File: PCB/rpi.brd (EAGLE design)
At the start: 75 x 70 mm, 63 parts, among them IC2 MC1541TO, IC4 MEGA16-A, X1 2526-

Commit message: On branch master 	modified:   PCB/eagle.epf 	modified:   PCB/rpi.brd 	modified:   RaspberryPI/RaspberryPI.pro.user
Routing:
- net GND: track 351.4 -> 365.5 mm
- removed copper zone on layer 1, net N$21
- removed copper zone on layer 16, net N$22
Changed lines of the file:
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@@
 <wire x1="30.45594375" y1="27.49915" x2="30.45594375" y2="24.921153125" width="1.016" layer="1"/>
 <wire x1="30.45594375" y1="24.921153125" x2="32.89613125" y2="22.480965625" width="1.016" layer="1"/>
-<wire x1="57.63515625" y1="25.98173125" x2="57.63515625" y2="21.321634375" width="2.1844" layer="1"/>
 <wire x1="30.45594375" y1="27.49915" x2="32.8984125" y2="29.94161875" width="1.016" layer="1"/>
 <wire x1="32.8984125" y1="29.94161875" x2="32.8984125" y2="33.282871875" width="1.016" layer="1"/>
@@
 <contactref element="C14" pad="-"/>
 <contactref element="C7" pad="-"/>
-<wire x1="57.55154375" y1="14.274546875" x2="57.571628125" y2="14.274546875" width="2.1844" layer="1"/>
-<wire x1="57.571628125" y1="14.274546875" x2="57.571628125" y2="21.25810625" width="2.1844" layer="1"/>
 <wire x1="57.523428125" y1="7.3449" x2="57.523428125" y2="14.24643125" width="2.1844" layer="1"/>
 <wire x1="57.523428125" y1="14.24643125" x2="57.55154375" y2="14.274546875" width="2.1844" layer="1"/>
-<wire x1="57.571628125" y1="21.25810625" x2="57.63515625" y2="21.321634375" width="0" layer="19" extent="1-1"/>
-<wire x1="42.1227" y1="18.626359375" x2="42.12465" y2="10.647703125" width="0" layer="19" extent="1-1"/>
+<wire x1="56.680578125" y1="20.36705625" x2="45.191290625" y2="20.36705625" width="2.1844" layer="1"/>
+<wire x1="45.191290625" y1="20.36705625" x2="44.300240625" y2="21.25810625" width="2.1844" layer="1"/>
+<wire x1="57.571628125" y1="14.29463125" x2="57.571628125" y2="21.25810625" width="2.1844" layer="1"/>
+<wire x1="57.63515625" y1="25.98173125" x2="57.63515625" y2="21.321634375" width="2.1844" layer="1"/>
+<wire x1="57.63515625" y1="21.321634375" x2="57.571628125" y2="21.25810625" width="2.1844" layer="1"/>
+<wire x1="57.571628125" y1="21.25810625" x2="56.680578125" y2="20.36705625" width="2.1844" layer="1"/>
 </signal>
 <signal name="+5V">
@@
 <wire x1="46.23093125" y1="44.331134375" x2="46.443821875" y2="44.544025" width="0.6096" layer="1"/>
 </signal>
-<signal name="N$21">
-<polygon width="0" layer="1" isolate="1.016" thermals="no" rank="6">
-<vertex x="0" y="70"/>
-<vertex x="75" y="70"/>
-<vertex x="75" y="0"/>
-<vertex x="0" y="0"/>
-</polygon>
-</signal>
-<signal name="N$22">
-<polygon width="0" layer="16" isolate="1.016" thermals="no" rank="6">
-<vertex x="0" y="70"/>
-<vertex x="75" y="70"/>
-<vertex x="75" y="0"/>
-<vertex x="0" y="0"/>
-</polygon>
-</signal>
 </signals>

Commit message: On branch master 	modified:   PCB/eagle.epf 	modified:   PCB/rpi.brd 	modified:   PCB/rpi.sch 	modified:   RaspberryPI/mainwindow.cpp 	modified:   RaspberryPI/mainwindow.h 	modified:   RaspberryPI/mainwindow.ui
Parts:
- U$14, U$2: device NX7002AK:SOT23 -> tablet:SOT23
- U$8: device max1811:SO8 -> tablet:SO8
- moved R4 4.52 mm to (17.4, 51.3), flipped to the top
- moved R10 2.56 mm to (13.9, 43.8), flipped to the bottom
- moved R3 0.60 mm to (15.8, 56.7), flipped to the top, turned to 0 degrees
- moved U$13 0.22 mm to (8.73, 58.9)
- flipped JP1 to the bottom
- flipped SV1 to the bottom
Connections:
- removed net N$24: SV1.6, X1.19
- removed net N$27: SV1.8, X1.24
- new net N$21: SV1.5, X1.19
- new net N$22: SV1.1, X1.23
- net +5V: now also U$1.D2, U$11.S, U$11.S2, U$11.S3, U$12.S, U$12.S2, U$12.S3, U$16.4, U$4.4, U$7.S, U$7.S2, U$7.S3, U$8.D2, U$8.G, U$8.S, U$8.S2, U$9.S, U$9.S2, U$9.S3; no longer U$1.P$7, U$11.P$1, U$11.P$2, U$11.P$3, U$12.P$1, U$12.P$2, U$12.P$3, U$16.P$4, U$4.P$4, U$7.P$1, U$7.P$2, U$7.P$3, U$8.EN, U$8.IN, U$8.SELI, U$8.SELV, U$9.P$1, U$9.P$2, U$9.P$3
- net GND: now also U$1.G, U$8.D3, U$8.S3; no longer U$1.P$4, U$8.GND, U$8.GND2
- net N$12: now also U$1.S2; no longer U$1.P$2
- net N$13: now also U$1.D4, U$3.1, U$3.2, U$3.3; no longer U$1.P$5, U$3.P$1, U$3.P$2, U$3.P$3
- net N$15: now also U$11.G, U$7.G; no longer U$11.P$4, U$7.P$4
- net N$17: now also U$16.1, U$16.3; no longer U$16.P$1, U$16.P$3
- net N$18: now also U$1.D3, U$3.4; no longer U$1.P$6, U$3.P$4
- net N$20: now also U$11.D, U$11.D2, U$11.D3, U$11.D4, U$7.D, U$7.D2, U$7.D3, U$7.D4; no longer U$11.P$5, U$11.P$6, U$11.P$7, U$11.P$8, U$7.P$5, U$7.P$6, U$7.P$7, U$7.P$8
- net N$23: now also U$3.5, U$4.1, U$4.3; no longer U$3.P$5, U$4.P$1, U$4.P$3
- net N$26: now also U$1.S3; no longer U$1.P$3
- net N$29: now also U$12.D, U$12.D2, U$12.D3, U$12.D4, U$9.D, U$9.D2, U$9.D3, U$9.D4; no longer U$12.P$5, U$12.P$6, U$12.P$7, U$12.P$8, U$9.P$5, U$9.P$6, U$9.P$7, U$9.P$8
- net N$4: now also SV1.3; no longer SV1.4
- net N$5: now also SV1.7, X1.24; no longer SV1.2, X1.23
- net PA3: now also U$1.D, U$8.D4; no longer U$1.P$8, U$8.BATT
- net PB4: now also SV1.8; no longer SV1.7
- net PB5: now also SV1.6; no longer SV1.5
- net PB6: now also SV1.4; no longer SV1.3
- net PC3: now also U$1.S; no longer U$1.P$1
- net PC4: now also U$12.G, U$9.G; no longer U$12.P$4, U$9.P$4
- net PD5: now also U$8.D; no longer U$8.!CHG
- net SCK: now also SV1.2; no longer SV1.1
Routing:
- net N$27: track 60.8 -> 0.00 mm
- net N$21: track 0.00 -> 34.1 mm
- net GND: track 365.5 -> 331.8 mm
- net N$5: track 29.6 -> 61.4 mm
- net N$22: track 0.00 -> 31.4 mm
- net N$24: track 30.5 -> 0.00 mm, vias 2 -> 0
- net N$4: track 6.54 -> 3.00 mm
- net N$7: track 11.9 -> 13.9 mm
- net RESET: track 58.5 -> 60.3 mm, vias 2 -> 1
- net +5V: track 257.4 -> 258.7 mm, vias 5 -> 4
- net N$1: track 39.3 -> 40.6 mm, vias 0 -> 2
- net PB6: track 14.7 -> 15.1 mm, vias 1 -> 0
- net SCK: track 16.5 -> 16.8 mm, vias 1 -> 0
- net N$8: track 25.9 -> 26.3 mm, vias 3 -> 2
- net PB5: vias 1 -> 0
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
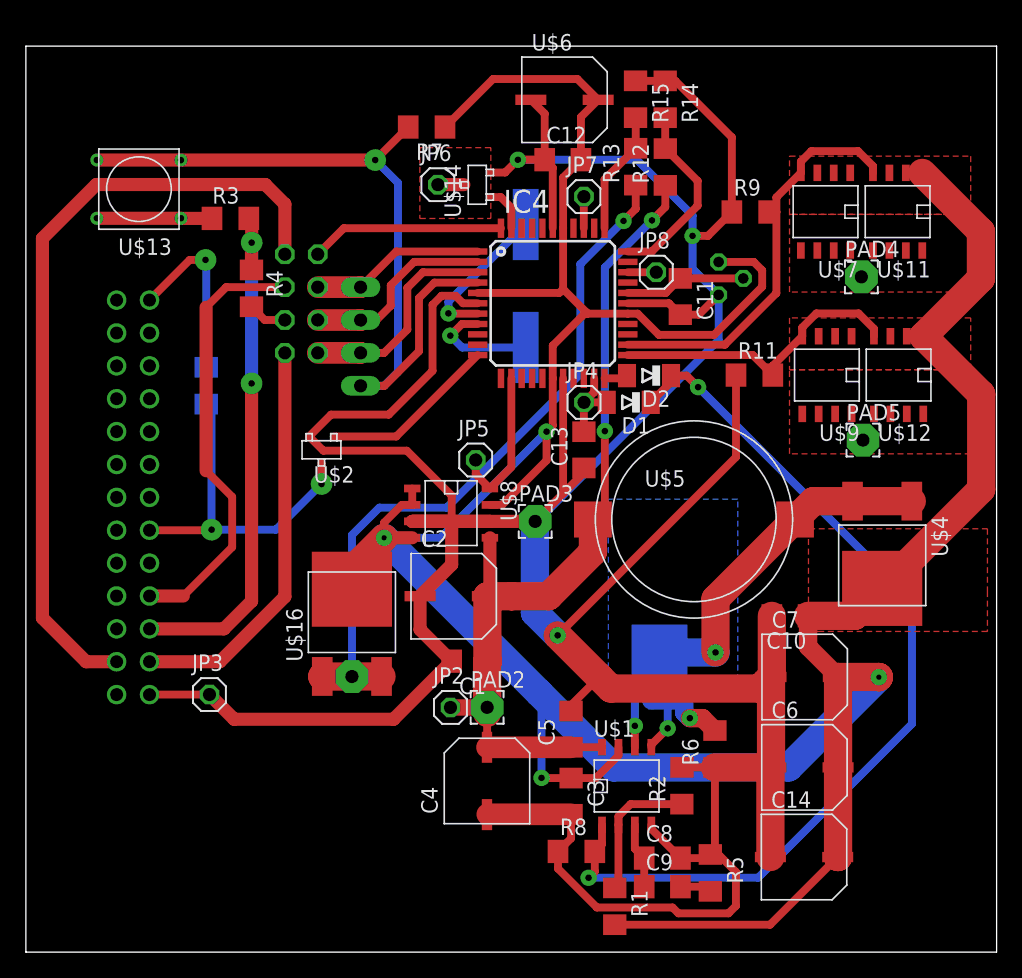
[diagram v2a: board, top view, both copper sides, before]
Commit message: On branch master 	modified:   PCB/eagle.epf 	modified:   PCB/rpi.brd 	modified:   PCB/rpi.sch
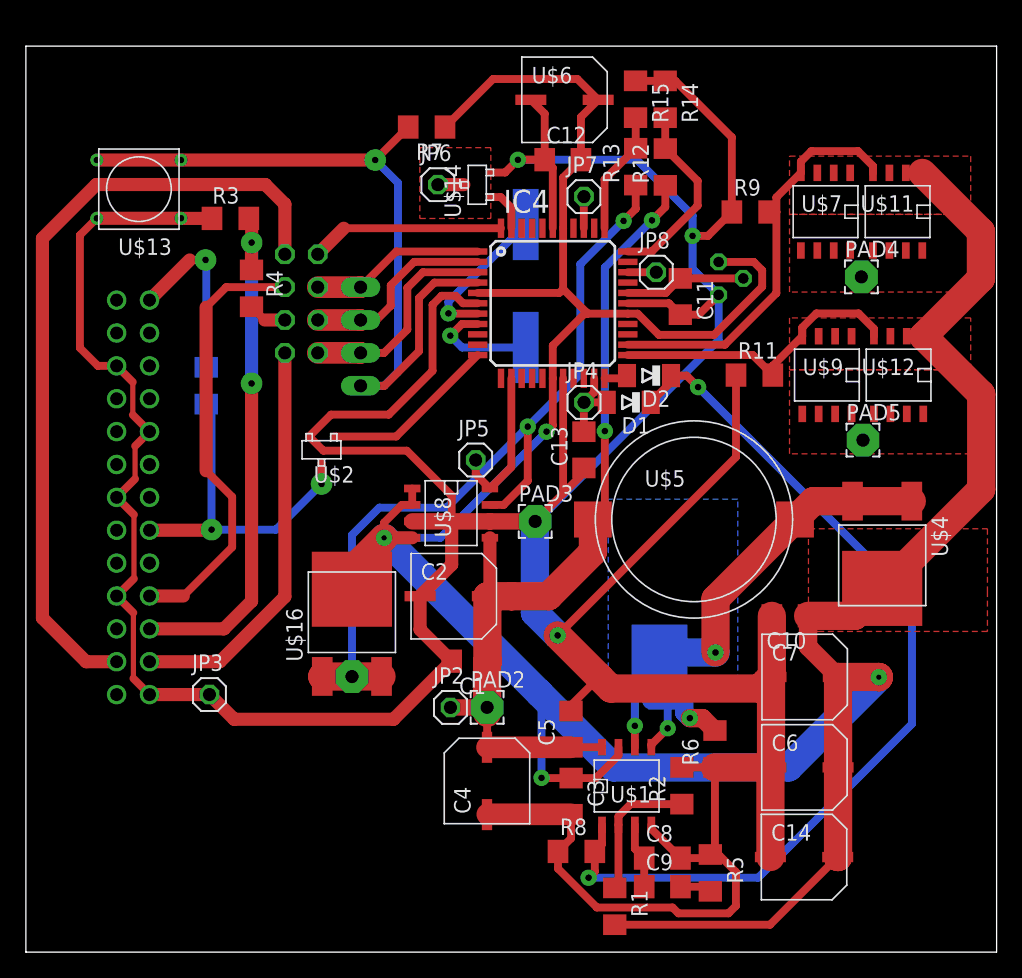
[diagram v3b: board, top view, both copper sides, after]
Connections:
- net +5V: no longer U$8.D2
- net N$17: now also U$8.D2
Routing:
- net GND: track 331.8 -> 375.4 mm
- net +5V: track 258.7 -> 250.7 mm
- net N$17: track 54.7 -> 62.6 mm, vias 1 -> 2
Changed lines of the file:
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@@
 <wire x1="21.887265625" y1="39.838325" x2="22.981690625" y2="38.7439" width="0.6096" layer="1"/>
 <wire x1="32.8984125" y1="35.27755625" x2="32.8984125" y2="33.282871875" width="0.6096" layer="1"/>
-<wire x1="29.85113125" y1="33.282871875" x2="35.853978125" y2="33.280025" width="1.016" layer="1"/>
-<wire x1="35.853978125" y1="33.280025" x2="39.328246875" y2="33.280025" width="1.016" layer="1"/>
+<wire x1="29.85113125" y1="33.282871875" x2="35.853978125" y2="33.280025" width="1.27" layer="1"/>
+<wire x1="35.853978125" y1="33.280025" x2="39.328246875" y2="33.280025" width="1.27" layer="1"/>
 <via x="39.328246875" y="33.280025" extent="1-16" drill="0.5" diameter="1.27"/>
 <wire x1="39.328246875" y1="33.280025" x2="39.3502125" y2="33.280025" width="1.016" layer="1"/>
@@
 <wire x1="57.571628125" y1="21.25810625" x2="56.680578125" y2="20.36705625" width="2.1844" layer="1"/>
 <wire x1="9.551828125" y1="19.8958875" x2="9.556715625" y2="19.900775" width="0.6096" layer="1"/>
-<wire x1="9.556715625" y1="19.900775" x2="14.182759375" y2="19.900775" width="0.6096" layer="1"/>
+<wire x1="9.556715625" y1="19.900775" x2="14.182759375" y2="19.900775" width="1.016" layer="1"/>
 <wire x1="11.982328125" y1="56.69913125" x2="11.991509375" y2="56.68995" width="0.6096" layer="1"/>
 <wire x1="11.991509375" y1="56.68995" x2="14.3805" y2="56.68995" width="1.016" layer="1"/>
@@
 <wire x1="22.981690625" y1="38.7439" x2="29.43206875" y2="38.7439" width="0.6096" layer="1"/>
 <wire x1="29.43206875" y1="38.7439" x2="32.8984125" y2="35.27755625" width="0.6096" layer="1"/>
+<wire x1="7.011828125" y1="45.2958875" x2="8.26085625" y2="44.046859375" width="0.6096" layer="1"/>
+<wire x1="8.26085625" y1="44.046859375" x2="8.26085625" y2="41.506859375" width="0.4064" layer="1"/>
+<wire x1="8.26085625" y1="41.506859375" x2="9.551828125" y2="40.2158875" width="0.6096" layer="1"/>
+<wire x1="9.551828125" y1="40.2158875" x2="8.438509375" y2="39.10256875" width="0.6096" layer="1"/>
+<wire x1="8.438509375" y1="39.10256875" x2="8.438509375" y2="36.56256875" width="0.4064" layer="1"/>
+<wire x1="8.438509375" y1="36.56256875" x2="7.011828125" y2="35.1358875" width="0.6096" layer="1"/>
+<wire x1="7.011828125" y1="35.1358875" x2="8.349684375" y2="33.79803125" width="0.6096" layer="1"/>
+<wire x1="8.349684375" y1="33.79803125" x2="8.349684375" y2="28.85374375" width="0.4064" layer="1"/>
+<wire x1="8.349684375" y1="28.85374375" x2="7.011828125" y2="27.5158875" width="0.6096" layer="1"/>
+<wire x1="7.011828125" y1="27.5158875" x2="8.30526875" y2="26.222446875" width="0.6096" layer="1"/>
+<wire x1="8.30526875" y1="26.222446875" x2="8.30526875" y2="21.142446875" width="0.4064" layer="1"/>
+<wire x1="8.30526875" y1="21.142446875" x2="9.551828125" y2="19.8958875" width="0.6096" layer="1"/>
+<wire x1="5.482328125" y1="56.69913125" x2="4.174840625" y2="55.39164375" width="0.6096" layer="1"/>
+<wire x1="4.174840625" y1="55.39164375" x2="4.174840625" y2="46.6826125" width="0.6096" layer="1"/>
+<wire x1="4.174840625" y1="46.6826125" x2="5.561565625" y2="45.2958875" width="0.6096" layer="1"/>
+<wire x1="5.561565625" y1="45.2958875" x2="7.011828125" y2="45.2958875" width="0.6096" layer="1"/>
 <wire x1="35.853978125" y1="33.280025" x2="35.85113125" y2="33.282871875" width="0" layer="19" extent="1-1"/>
-<wire x1="7.011828125" y1="27.5158875" x2="9.551828125" y2="19.8958875" width="0" layer="19" extent="1-1"/>
-<wire x1="7.011828125" y1="35.1358875" x2="7.011828125" y2="27.5158875" width="0" layer="19" extent="1-1"/>
-<wire x1="9.551828125" y1="40.2158875" x2="7.011828125" y2="35.1358875" width="0" layer="19" extent="1-1"/>
-<wire x1="7.011828125" y1="45.2958875" x2="9.551828125" y2="40.2158875" width="0" layer="19" extent="1-1"/>
-<wire x1="5.482328125" y1="56.69913125" x2="7.011828125" y2="45.2958875" width="0" layer="19" extent="1-1"/>
 </signal>
 <signal name="+5V">
@@
 <contactref element="U$7" pad="S"/>
 <contactref element="U$11" pad="S"/>
-<contactref element="U$8" pad="D2"/>
-<wire x1="35.85113125" y1="34.552871875" x2="36.791025" y2="34.552871875" width="0.6096" layer="1"/>
-<wire x1="36.791025" y1="34.552871875" x2="40.228184375" y2="37.99003125" width="0.6096" layer="1"/>
-<wire x1="40.228184375" y1="37.99003125" x2="40.228184375" y2="40.21331875" width="0.6096" layer="1"/>
 <contactref element="U$1" pad="D2"/>
 <contactref element="C3" pad="1"/>
@@
 <contactref element="R4" pad="2"/>
 <contactref element="SV1" pad="3"/>
-<wire x1="20.0098125" y1="48.839659375" x2="18.453003125" y2="48.839659375" width="0.6096" layer="1"/>
+<wire x1="20.0098125" y1="48.839659375" x2="18.453003125" y2="48.839659375" width="1.016" layer="1"/>
 <wire x1="18.453003125" y1="48.839659375" x2="17.429975" y2="49.8626875" width="0.6096" layer="1"/>
 </signal>
@@
 <contactref element="X1" pad="15"/>
 <contactref element="R10" pad="1"/>
-<wire x1="9.551828125" y1="32.5958875" x2="14.30258125" y2="32.5958875" width="0.6096" layer="1"/>
+<wire x1="9.551828125" y1="32.5958875" x2="14.30258125" y2="32.5958875" width="1.016" layer="1"/>
 <wire x1="14.30258125" y1="32.5958875" x2="14.34669375" y2="32.64" width="0.6096" layer="1"/>
 <via x="14.34669375" y="32.64" extent="1-16" drill="0.5" diameter="1.6764"/>
@@
 <contactref element="SV1" pad="8"/>
 <wire x1="36.707703125" y1="55.931134375" x2="24.5612875" y2="55.931134375" width="0.6096" layer="1"/>
-<wire x1="24.5612875" y1="55.931134375" x2="22.5498125" y2="53.919659375" width="0.6096" layer="1"/>
+<wire x1="24.5612875" y1="55.931134375" x2="22.5498125" y2="53.919659375" width="1.016" layer="1"/>
 </signal>
 <signal name="PC4">
@@
 <via x="13.880534375" y="53.480428125" extent="1-16" drill="0.5" diameter="1.6764"/>
 <wire x1="13.880534375" y1="53.480428125" x2="12.65636875" y2="53.480428125" width="0.6096" layer="1"/>
-<wire x1="12.65636875" y1="53.480428125" x2="9.551828125" y2="50.3758875" width="0.6096" layer="1"/>
+<wire x1="12.65636875" y1="53.480428125" x2="9.551828125" y2="50.3758875" width="1.016" layer="1"/>
 </signal>
 <signal name="N$9">
@@
 <wire x1="46.18034375" y1="56.49406875" x2="42.837009375" y2="53.150734375" width="0.6096" layer="16"/>
 <wire x1="42.837009375" y1="53.150734375" x2="42.837009375" y2="44.664734375" width="0.6096" layer="16"/>
-<wire x1="42.837009375" y1="44.664734375" x2="32.5148375" y2="34.3425625" width="0.6096" layer="16"/>
+<wire x1="42.837009375" y1="44.664734375" x2="38.775484375" y2="40.603209375" width="0.6096" layer="16"/>
+<wire x1="38.38693125" y1="40.21465625" x2="32.5148375" y2="34.3425625" width="0.6096" layer="16"/>
 <wire x1="32.5148375" y1="34.3425625" x2="27.306790625" y2="34.3425625" width="0.6096" layer="16"/>
 <wire x1="27.306790625" y1="34.3425625" x2="25.194615625" y2="32.2303875" width="0.6096" layer="16"/>
 <wire x1="25.194615625" y1="32.2303875" x2="25.194615625" y2="21.293346875" width="0.6096" layer="16"/>
+<contactref element="U$8" pad="D2"/>
+<wire x1="35.85113125" y1="34.552871875" x2="36.912434375" y2="34.552871875" width="0.6096" layer="1"/>
+<wire x1="36.912434375" y1="34.552871875" x2="38.775484375" y2="36.415921875" width="0.6096" layer="1"/>
+<wire x1="38.775484375" y1="36.415921875" x2="38.775484375" y2="40.603209375" width="0.6096" layer="1"/>
+<via x="38.775484375" y="40.603209375" extent="1-16" drill="0.5" diameter="1.27"/>
+<wire x1="38.775484375" y1="40.603209375" x2="38.38693125" y2="40.21465625" width="0.6096" layer="16"/>
 </signal>
 <signal name="N$19">

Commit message: On branch master 	modified:   PCB/eagle.epf 	modified:   PCB/rpi.brd 	modified:   PCB/rpi.sch 	modified:   RaspberryPI-shutdown/RaspberryPI-shutdown.pro 	modified:   RaspberryPI/RaspberryPI.pro
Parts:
- JP1: device con-lstb:MA04-1 -> tablet:MA04-1
- SV1: device con-lstb:MA04-2 -> tablet:MA04-2
- X1: device con-3m:PAK100/2500-26 -> tablet:PAK100/2500-26
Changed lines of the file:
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@@
 <element name="R3" library="resistor" package="R1206" value="3000" x="15.8025" y="56.68995"/>
 <element name="R4" library="resistor" package="R1206" value="2000" x="17.429975" y="51.2846875" rot="R270"/>
-<element name="JP1" library="con-lstb" package="MA04-1" value="" x="25.861009375" y="47.56710625" rot="MR90">
+<element name="JP1" library="tablet" package="MA04-1" value="" x="25.861009375" y="47.56710625" rot="MR90">
 <attribute name="OC_NEWARK" value="unknown" x="25.861009375" y="47.56710625" size="1.778" layer="28" rot="MR90" display="off"/>
 <attribute name="MPN" value="" x="25.861009375" y="47.56710625" size="1.778" layer="28" rot="MR90" display="off"/>
@@
 <attribute name="OC_FARNELL" value="unknown" x="25.861009375" y="47.56710625" size="1.778" layer="28" rot="MR90" display="off"/>
 </element>
-<element name="X1" library="con-3m" package="PAK100/2500-26" value="2526-" x="8.281828125" y="35.1358875" rot="MR270">
+<element name="X1" library="tablet" package="PAK100/2500-26" value="2526-" x="8.281828125" y="35.1358875" rot="MR270">
 <attribute name="OC_NEWARK" value="unknown" x="8.281828125" y="35.1358875" size="1.778" layer="28" rot="MR270" display="off"/>
 <attribute name="MPN" value="" x="8.281828125" y="35.1358875" size="1.778" layer="28" rot="MR270" display="off"/>
@@
 <attribute name="OC_FARNELL" value="unknown" x="8.281828125" y="35.1358875" size="1.778" layer="28" rot="MR270" display="off"/>
 </element>
-<element name="SV1" library="con-lstb" package="MA04-2" value="" x="21.2798125" y="50.109659375" rot="MR90">
+<element name="SV1" library="tablet" package="MA04-2" value="" x="21.2798125" y="50.109659375" rot="MR90">
 <attribute name="OC_NEWARK" value="unknown" x="21.2798125" y="50.109659375" size="1.778" layer="28" rot="MR90" display="off"/>
 <attribute name="MPN" value="" x="21.2798125" y="50.109659375" size="1.778" layer="28" rot="MR90" display="off"/>
